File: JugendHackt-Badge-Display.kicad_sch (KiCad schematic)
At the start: 142 parts, among them J1 USB_C_Receptacle_USB2.0, J2 Conn_01x30_Female, J3 Conn_01x02, Q1 S8050, Q2 S8050, SW1 K1-1506SN-01, SW2 SW_Push, SW3 SW_Push, SW4 SW_SPDT, U1 RM-V8xxC_TR1, U2 SRV05-4, U3 CH340C, U4 ESP32-WROOM-32, U5 SDB628, U6 TLV62568DBV, U7 MCP73831-2-OT

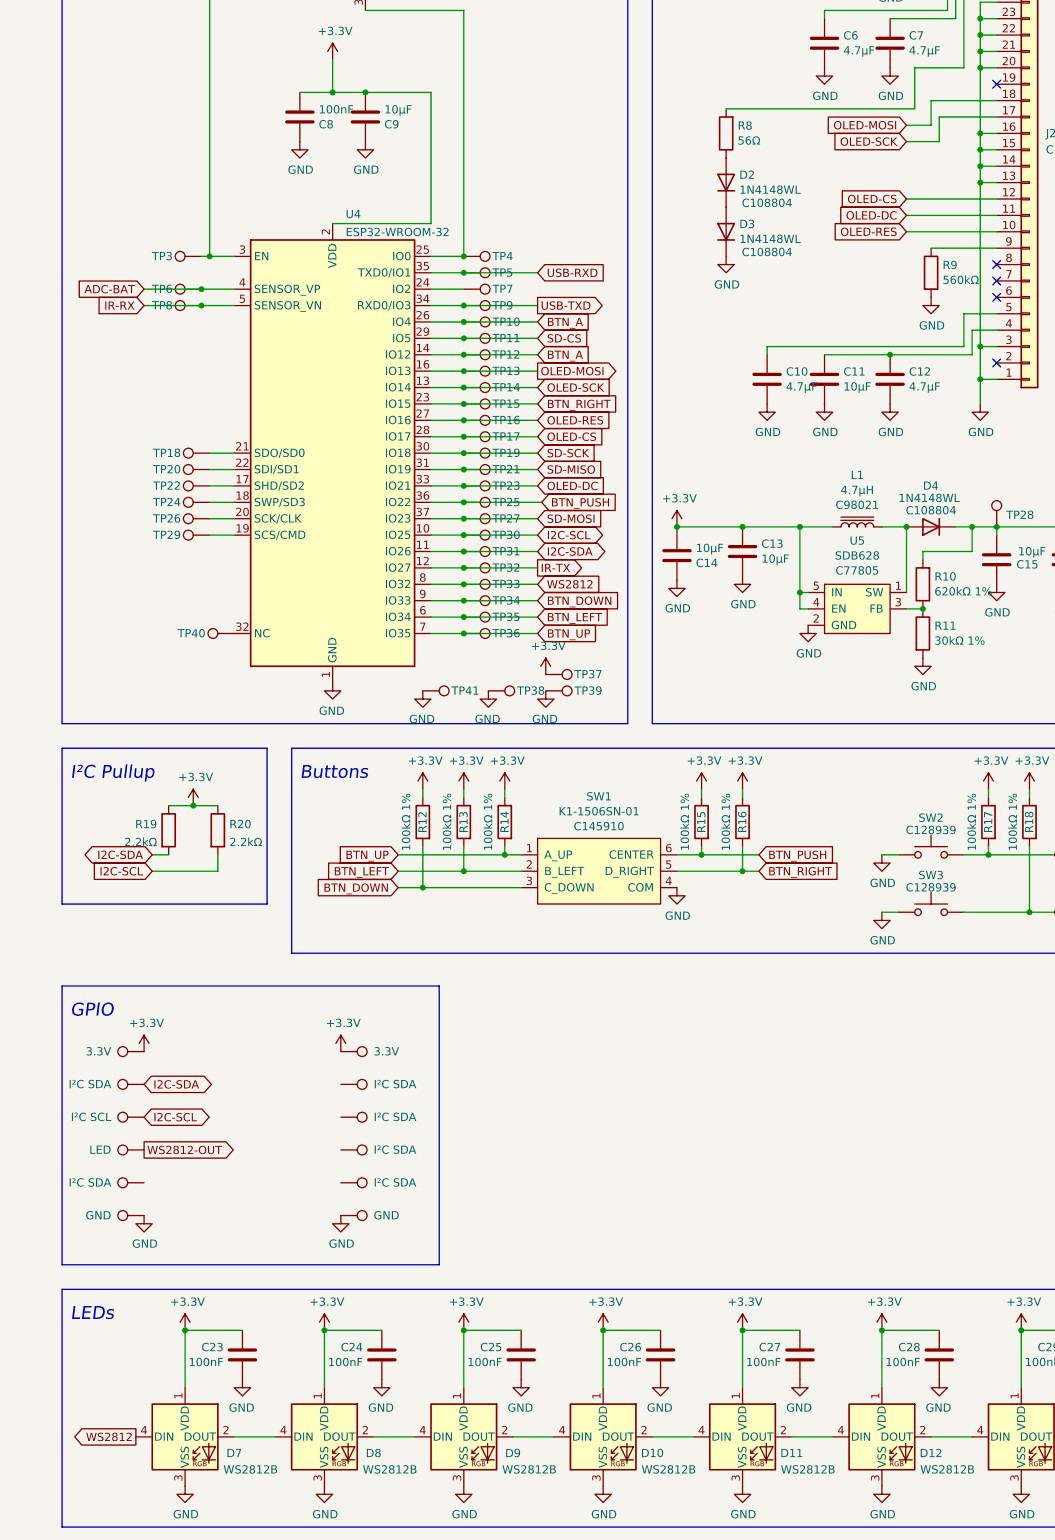
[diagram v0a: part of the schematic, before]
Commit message: feat: Finalize SCH, changes in PCB
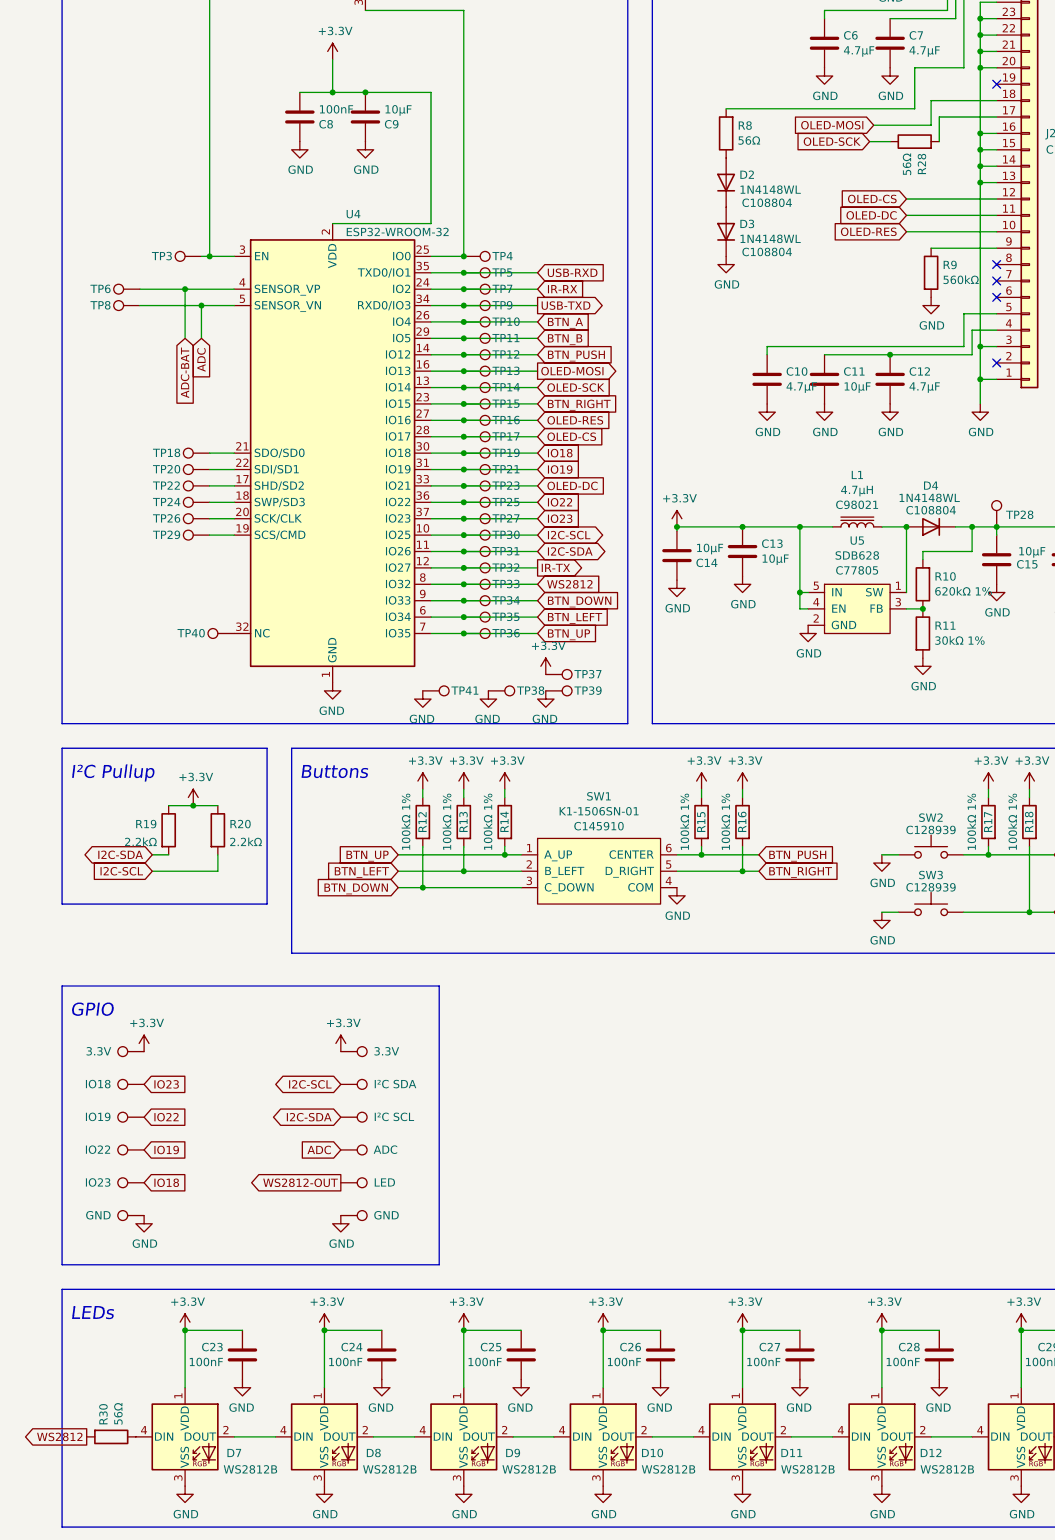
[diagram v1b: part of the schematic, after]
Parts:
- added R28, R30: 56Ω, Resistor_SMD:R_0603_1608Metric, symbol Device:R
- IO10: value I²C SDA -> LED
- IO3: value I²C SDA -> IO18
- IO5: value I²C SCL -> IO19
- IO6: value I²C SDA -> I²C SCL
- IO7: value LED -> IO22
- IO8: value I²C SDA -> ADC
- IO9: value I²C SDA -> IO23
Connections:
- net SD-CS is gone; now on net BTN_B: TP11.1, U4.29 (IO5)
- net SD-SCK is gone; now on net IO18: TP19.1, U4.30 (IO18)
- net BTN_A: no longer TP12.1, U4.14 (IO12)
- net BTN_PUSH: now also TP12.1, U4.14 (IO12); no longer TP25.1, U4.36 (IO22)
- net I2C-SCL: now also IO4.1; no longer IO5.1
- net I2C-SDA: now also IO6.1; no longer IO3.1
- net IR-RX: now also TP7.1, U4.24 (IO2); no longer TP8.1, U4.5 (SENSOR_VN)
- net OLED-SCK: now also R28.1; no longer J2.17 (Pin_17)
- net WS2812: now also R30.2; no longer D7.4 (DIN)
- net WS2812-OUT: now also IO10.1; no longer IO7.1
- net ADC: now reaches IO8.1
- net ADC: now also TP8.1, U4.5 (SENSOR_VN)
- net IO18: now reaches IO9.1
- net SD-MISO renamed IO19
- net IO19: now also IO7.1
- net SD-MOSI renamed IO23
- net IO23: now also IO3.1
- new net: J2.17 (Pin_17), R28.2
- new net: D7.4 (DIN), R30.1
- new net IO22: IO5.1, TP25.1, U4.36 (IO22)
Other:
- moved on the sheet: TP6, TP8

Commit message: feat: Finalize PCB & SCH
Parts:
- C23, C24, C25, C26, C27, C28, C29: JLC 0603 -> (none)
- D1: footprint Teebeutel_Special_Parts:LKIR30102C -> Caffeinated Labs:LKIR30102C
- D10, D11, D12, D13, D7, D8, D9: footprint JugendHackt:LED_WS2812B-Backlight -> Caffeinated Labs:WS2812B-4020
- IO4: value I²C SDA -> SCL
- IO6: value I²C SCL -> SDA
- SW1: footprint Teebeutel_Special_Parts:K1-1506SN-01 -> Caffeinated Labs:K1-1506SN-01
- U1: footprint Teebeutel_Special_Parts:IRM-V8xxC-TR1 -> Caffeinated Labs:IRM-V8xxC-TR1
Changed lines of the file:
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@@
       (effects (font (size 1.27 1.27)) hide)
     )
-    (property "JLC" "0603" (id 4) (at 172.72 255.27 0)
+    (property "JLC" "" (id 4) (at 172.72 255.27 0)
       (effects (font (size 1.27 1.27)) hide)
     )
@@
       (effects (font (size 1.27 1.27)) hide)
     )
-    (property "JLC" "0603" (id 4) (at 151.13 255.27 0)
+    (property "JLC" "" (id 4) (at 151.13 255.27 0)
       (effects (font (size 1.27 1.27)) hide)
     )
@@
       (effects (font (size 1.27 1.27)) hide)
     )
-    (property "JLC" "0603" (id 4) (at 129.54 255.27 0)
+    (property "JLC" "" (id 4) (at 129.54 255.27 0)
       (effects (font (size 1.27 1.27)) hide)
     )
@@
       (effects (font (size 1.27 1.27)) hide)
     )
-    (property "JLC" "0603" (id 4) (at 107.95 255.27 0)
+    (property "JLC" "" (id 4) (at 107.95 255.27 0)
       (effects (font (size 1.27 1.27)) hide)
     )
@@
       (effects (font (size 1.27 1.27)) hide)
     )
-    (property "JLC" "0603" (id 4) (at 43.18 255.27 0)
+    (property "JLC" "" (id 4) (at 43.18 255.27 0)
       (effects (font (size 1.27 1.27)) hide)
     )
@@
     (property "Reference" "D12" (id 0) (at 149.86 270.51 0))
     (property "Value" "WS2812B" (id 1) (at 152.4 273.05 0))
-    (property "Footprint" "JugendHackt:LED_WS2812B-Backlight" (id 2) (at 143.51 275.59 0)
+    (property "Footprint" "Caffeinated Labs:WS2812B-4020" (id 2) (at 143.51 275.59 0)
       (effects (font (size 1.27 1.27)) (justify left top) hide)
     )
@@
     (property "Reference" "D9" (id 0) (at 85.09 270.51 0))
     (property "Value" "WS2812B" (id 1) (at 87.63 273.05 0))
-    (property "Footprint" "JugendHackt:LED_WS2812B-Backlight" (id 2) (at 78.74 275.59 0)
+    (property "Footprint" "Caffeinated Labs:WS2812B-4020" (id 2) (at 78.74 275.59 0)
       (effects (font (size 1.27 1.27)) (justify left top) hide)
     )
@@
     (property "Reference" "D11" (id 0) (at 128.27 270.51 0))
     (property "Value" "WS2812B" (id 1) (at 130.81 273.05 0))
-    (property "Footprint" "JugendHackt:LED_WS2812B-Backlight" (id 2) (at 121.92 275.59 0)
+    (property "Footprint" "Caffeinated Labs:WS2812B-4020" (id 2) (at 121.92 275.59 0)
       (effects (font (size 1.27 1.27)) (justify left top) hide)
     )
@@
       (effects (font (size 1.27 1.27)) hide)
     )
-    (property "JLC" "0603" (id 4) (at 86.36 255.27 0)
+    (property "JLC" "" (id 4) (at 86.36 255.27 0)
       (effects (font (size 1.27 1.27)) hide)
     )
@@
       (effects (font (size 1.27 1.27)) (justify left) hide)
     )
-    (property "Value" "I²C SDA" (id 1) (at 63.5 213.36 90)
+    (property "Value" "SCL" (id 1) (at 63.5 213.36 90)
       (effects (font (size 1.27 1.27)) (justify left))
     )
@@
       (effects (font (size 1.27 1.27)) (justify left) hide)
     )
-    (property "Value" "I²C SCL" (id 1) (at 63.5 218.44 90)
+    (property "Value" "SDA" (id 1) (at 63.5 218.44 90)
       (effects (font (size 1.27 1.27)) (justify left))
     )
@@
     (property "Reference" "D10" (id 0) (at 106.68 270.51 0))
     (property "Value" "WS2812B" (id 1) (at 109.22 273.05 0))
-    (property "Footprint" "JugendHackt:LED_WS2812B-Backlight" (id 2) (at 100.33 275.59 0)
+    (property "Footprint" "Caffeinated Labs:WS2812B-4020" (id 2) (at 100.33 275.59 0)
       (effects (font (size 1.27 1.27)) (justify left top) hide)
     )
@@
       (effects (font (size 1.27 1.27)) hide)
     )
-    (property "JLC" "0603" (id 4) (at 64.77 255.27 0)
+    (property "JLC" "" (id 4) (at 64.77 255.27 0)
       (effects (font (size 1.27 1.27)) hide)
     )
@@
     (property "Reference" "D7" (id 0) (at 41.91 270.51 0))
     (property "Value" "WS2812B" (id 1) (at 44.45 273.05 0))
-    (property "Footprint" "JugendHackt:LED_WS2812B-Backlight" (id 2) (at 35.56 275.59 0)
+    (property "Footprint" "Caffeinated Labs:WS2812B-4020" (id 2) (at 35.56 275.59 0)
       (effects (font (size 1.27 1.27)) (justify left top) hide)
     )
@@
     (property "Reference" "U1" (id 0) (at 205.74 25.019 0))
     (property "Value" "RM-V8xxC_TR1" (id 1) (at 205.74 27.3304 0))
-    (property "Footprint" "Teebeutel_Special_Parts:IRM-V8xxC-TR1" (id 2) (at 205.74 27.94 0)
+    (property "Footprint" "Caffeinated Labs:IRM-V8xxC-TR1" (id 2) (at 205.74 27.94 0)
       (effects (font (size 1.27 1.27)) hide)
     )
@@
     (property "Reference" "D1" (id 0) (at 213.5378 48.387 0))
     (property "Value" "LED-IR" (id 1) (at 213.5378 50.6984 0))
-    (property "Footprint" "Teebeutel_Special_Parts:LKIR30102C" (id 2) (at 213.36 57.15 0)
+    (property "Footprint" "Caffeinated Labs:LKIR30102C" (id 2) (at 213.36 57.15 0)
       (effects (font (size 1.27 1.27)) hide)
     )
@@
     (property "Reference" "D8" (id 0) (at 63.5 270.51 0))
     (property "Value" "WS2812B" (id 1) (at 66.04 273.05 0))
-    (property "Footprint" "JugendHackt:LED_WS2812B-Backlight" (id 2) (at 57.15 275.59 0)
+    (property "Footprint" "Caffeinated Labs:WS2812B-4020" (id 2) (at 57.15 275.59 0)
       (effects (font (size 1.27 1.27)) (justify left top) hide)
     )
@@
     (property "Reference" "D13" (id 0) (at 171.45 270.51 0))
     (property "Value" "WS2812B" (id 1) (at 173.99 273.05 0))
-    (property "Footprint" "JugendHackt:LED_WS2812B-Backlight" (id 2) (at 165.1 275.59 0)
+    (property "Footprint" "Caffeinated Labs:WS2812B-4020" (id 2) (at 165.1 275.59 0)
       (effects (font (size 1.27 1.27)) (justify left top) hide)
     )
@@
     (property "Reference" "SW1" (id 0) (at 98.425 168.783 0))
     (property "Value" "K1-1506SN-01" (id 1) (at 98.425 171.0944 0))
-    (property "Footprint" "Teebeutel_Special_Parts:K1-1506SN-01" (id 2) (at 99.06 173.99 0)
+    (property "Footprint" "Caffeinated Labs:K1-1506SN-01" (id 2) (at 99.06 173.99 0)
       (effects (font (size 1.27 1.27)) hide)
     )
@@
     )
     (path "/dd33b81c-76e2-40ae-b39f-e89236b48a06"
-      (reference "D1") (unit 1) (value "LED-IR") (footprint "Teebeutel_Special_Parts:LKIR30102C")
+      (reference "D1") (unit 1) (value "LED-IR") (footprint "Caffeinated Labs:LKIR30102C")
     )
     (path "/65f7348d-4bcd-4f43-a175-d822022803c9"
@@
     )
     (path "/bf85be0d-1805-42bc-abe9-efe63556cfcc"
-      (reference "D7") (unit 1) (value "WS2812B") (footprint "JugendHackt:LED_WS2812B-Backlight")
+      (reference "D7") (unit 1) (value "WS2812B") (footprint "Caffeinated Labs:WS2812B-4020")
     )
     (path "/e5606b3f-dfc0-4c24-910f-a704585b5473"
-      (reference "D8") (unit 1) (value "WS2812B") (footprint "JugendHackt:LED_WS2812B-Backlight")
+      (reference "D8") (unit 1) (value "WS2812B") (footprint "Caffeinated Labs:WS2812B-4020")
     )
     (path "/86bd34fa-a19d-47f6-a943-c3441c21389a"
-      (reference "D9") (unit 1) (value "WS2812B") (footprint "JugendHackt:LED_WS2812B-Backlight")
+      (reference "D9") (unit 1) (value "WS2812B") (footprint "Caffeinated Labs:WS2812B-4020")
     )
     (path "/b648339a-edcc-4138-bdf4-4222d1fdf910"
-      (reference "D10") (unit 1) (value "WS2812B") (footprint "JugendHackt:LED_WS2812B-Backlight")
+      (reference "D10") (unit 1) (value "WS2812B") (footprint "Caffeinated Labs:WS2812B-4020")
     )
     (path "/8f4ef546-62b7-4645-ac5a-8d039ca7bbee"
-      (reference "D11") (unit 1) (value "WS2812B") (footprint "JugendHackt:LED_WS2812B-Backlight")
+      (reference "D11") (unit 1) (value "WS2812B") (footprint "Caffeinated Labs:WS2812B-4020")
     )
     (path "/815ec5e4-75b5-412f-a424-95f7877e0353"
-      (reference "D12") (unit 1) (value "WS2812B") (footprint "JugendHackt:LED_WS2812B-Backlight")
+      (reference "D12") (unit 1) (value "WS2812B") (footprint "Caffeinated Labs:WS2812B-4020")
     )
     (path "/f004c71d-a9bd-4acb-9645-74dfd08e3bbd"
-      (reference "D13") (unit 1) (value "WS2812B") (footprint "JugendHackt:LED_WS2812B-Backlight")
+      (reference "D13") (unit 1) (value "WS2812B") (footprint "Caffeinated Labs:WS2812B-4020")
     )
     (path "/15945701-c8fb-4b60-b7d0-b0cf6779dbff"
@@
     )
     (path "/9cf66541-357c-4ac2-9f97-60b9ae87efbf"
-      (reference "IO4") (unit 1) (value "I²C SDA") (footprint "Caffeinated Labs:LabConnector_4mm")
+      (reference "IO4") (unit 1) (value "SCL") (footprint "Caffeinated Labs:LabConnector_4mm")
     )
     (path "/d31f1d0a-bf51-4c60-a0cd-423e75cbbc16"
@@
     )
     (path "/aaf04f05-39ed-44ab-9e62-3c8d06a6f73f"
-      (reference "IO6") (unit 1) (value "I²C SCL") (footprint "Caffeinated Labs:LabConnector_4mm")
+      (reference "IO6") (unit 1) (value "SDA") (footprint "Caffeinated Labs:LabConnector_4mm")
     )
     (path "/4d01cea8-bc1f-4b6b-832e-88da195198d2"
@@
     )
     (path "/f3395e3d-f144-4b53-b8e7-e3fd27accf9c"
-      (reference "SW1") (unit 1) (value "K1-1506SN-01") (footprint "Teebeutel_Special_Parts:K1-1506SN-01")
+      (reference "SW1") (unit 1) (value "K1-1506SN-01") (footprint "Caffeinated Labs:K1-1506SN-01")
     )
     (path "/9ac73438-3868-4100-8bb1-44c6fc649b21"
@@
     )
     (path "/cef15525-ad72-4ac9-af89-dd96f9bf5e8a"
-      (reference "U1") (unit 1) (value "RM-V8xxC_TR1") (footprint "Teebeutel_Special_Parts:IRM-V8xxC-TR1")
+      (reference "U1") (unit 1) (value "RM-V8xxC_TR1") (footprint "Caffeinated Labs:IRM-V8xxC-TR1")
     )
     (path "/2203db93-6422-4447-9ce4-6a51fbcac5f2"

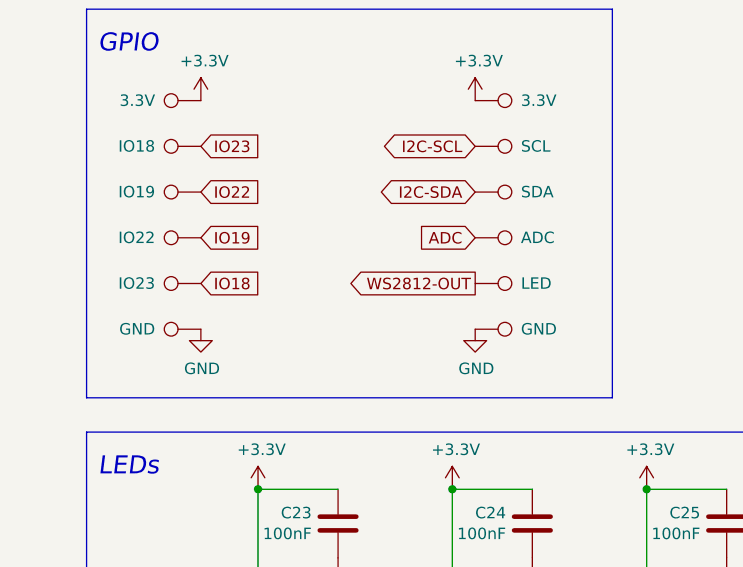
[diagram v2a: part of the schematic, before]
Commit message: changed IO layout
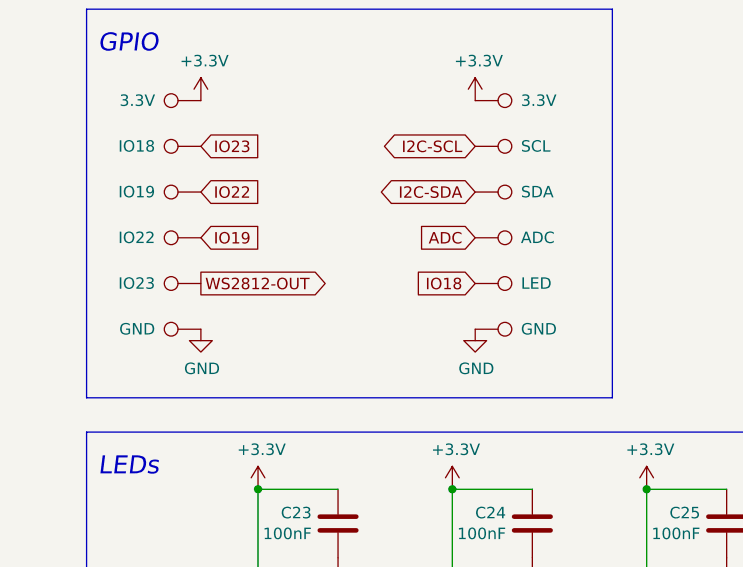
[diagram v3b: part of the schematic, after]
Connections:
- net IO18: now also IO10.1; no longer IO9.1
- net WS2812-OUT: now also IO9.1; no longer IO10.1
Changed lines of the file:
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@@
     )
   )
-  (global_label "WS2812-OUT" (shape output) (at 58.42 228.6 180) (fields_autoplaced)
-    (effects (font (size 1.27 1.27)) (justify right))
-    (property "Intersheet References" "${INTERSHEET_REFS}" (id 0) (at 43.3069 228.6794 0)
-      (effects (font (size 1.27 1.27)) (justify right) hide)
+  (global_label "WS2812-OUT" (shape output) (at 27.94 228.6 0) (fields_autoplaced)
+    (effects (font (size 1.27 1.27)) (justify left))
+    (property "Intersheet References" "${INTERSHEET_REFS}" (id 0) (at 43.0531 228.5206 0)
+      (effects (font (size 1.27 1.27)) (justify left) hide)
     )
   )
@@
     )
   )
-  (global_label "IO18" (shape input) (at 27.94 228.6 0) (fields_autoplaced)
-    (effects (font (size 1.27 1.27)) (justify left))
-    (property "Intersheet References" "${INTERSHEET_REFS}" (id 0) (at 34.7074 228.5206 0)
-      (effects (font (size 1.27 1.27)) (justify left) hide)
-    )
-  )
+  (global_label "IO18" (shape input) (at 58.42 228.6 180) (fields_autoplaced)
+    (effects (font (size 1.27 1.27)) (justify right))
+    (property "Intersheet References" "${INTERSHEET_REFS}" (id 0) (at 51.6526 228.6794 0)
+      (effects (font (size 1.27 1.27)) (justify right) hide)
+    )
+  )

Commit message: feat: finalized PCB
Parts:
- removed C26: 100nF, Capacitor_SMD:C_0603_1608Metric, symbol Device:C
- removed D10: WS2812B, Caffeinated Labs:WS2812B-4020, symbol LED:WS2812B
- removed TP1: IR-RX, TestPoint:TestPoint_Pad_D1.0mm, symbol Connector:TestPoint
- removed TP2: IR-TX, TestPoint:TestPoint_Pad_D1.0mm, symbol Connector:TestPoint
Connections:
- net at D9.2 (DOUT): now also D11.4 (DIN)
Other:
- moved on the sheet: C23, C24, C25, C27, C28, C29, D11, D12, D13, D7, D8, D9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
